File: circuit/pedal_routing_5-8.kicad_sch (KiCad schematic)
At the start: 12 parts, among them U601 CD4051B, U602 CD4051B, U603 CD4051B, U604 CD4051B

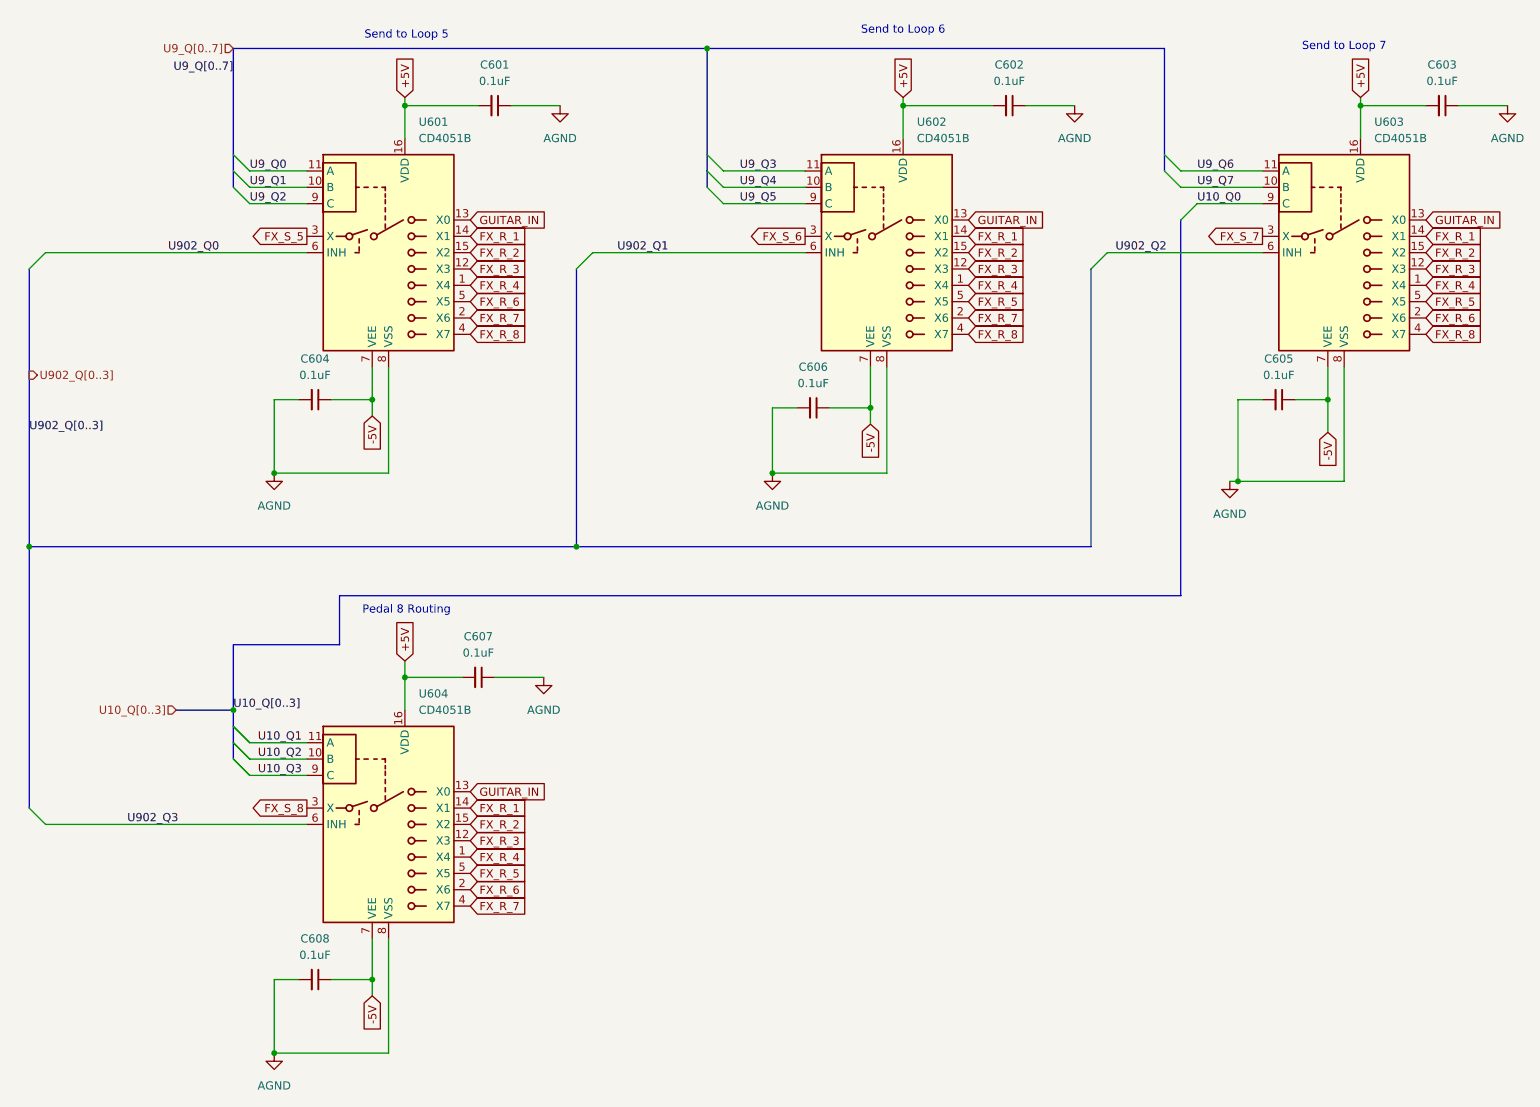
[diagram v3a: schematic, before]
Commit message: Added ferrite beads and tweaked PCB
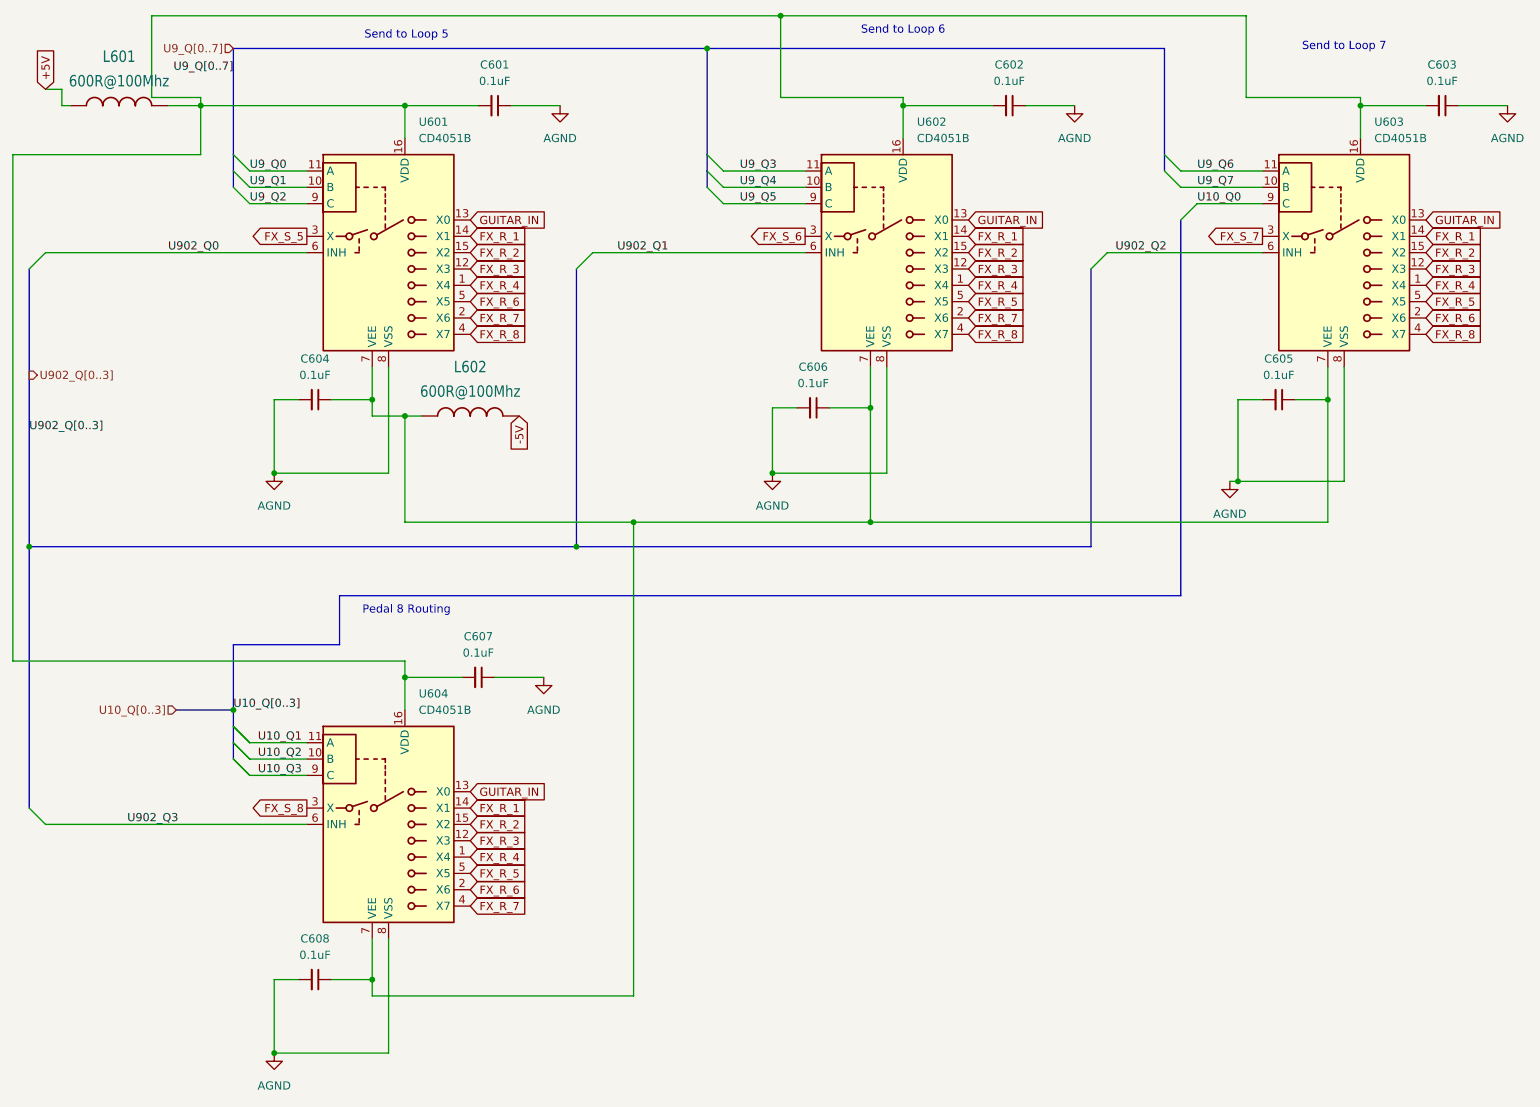
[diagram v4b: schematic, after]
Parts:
- added L601, L602: 600R@100Mhz, WE-UKW:WE-UKW_74275010, symbol WE_UKW:WE-UKW_1SW_74275010
- C601, C602, C603, C604, C605, C606, C607, C608: footprint Capacitor_THT:C_Axial_L3.8mm_D2.6mm_P7.50mm_Horizontal -> Capacitor_THT:C_Disc_D3.0mm_W2.0mm_P2.50mm
- U601, U602, U603, U604: footprint Package_DIP:CERDIP-16_W7.62mm_SideBrazed -> Package_DIP:DIP-16_W7.62mm
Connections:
- net +5V: now also L601.1; no longer C601.2, C602.2, C603.2, C607.2, U601.16 (VDD), U602.16 (VDD), U603.16 (VDD), U604.16 (VDD)
- net -5V: now also L602.2; no longer C604.1, C605.1, C606.1, C608.1, U601.7 (VEE), U602.7 (VEE), U603.7 (VEE), U604.7 (VEE)
- new net: C601.2, C602.2, C603.2, C607.2, L601.2, U601.16 (VDD), U602.16 (VDD), U603.16 (VDD), U604.16 (VDD)
- new net: C604.1, C605.1, C606.1, C608.1, L602.1, U601.7 (VEE), U602.7 (VEE), U603.7 (VEE), U604.7 (VEE)

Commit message: Circuit tweaks and PCB
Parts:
- C601: renamed from C604; footprint Capacitor_THT:C_Disc_D3.0mm_W2.0mm_P2.50mm -> Capacitor_THT:C_Disc_D5.0mm_W2.5mm_P2.50mm
- C602: renamed from C608; footprint Capacitor_THT:C_Disc_D3.0mm_W2.0mm_P2.50mm -> Capacitor_THT:C_Disc_D5.0mm_W2.5mm_P2.50mm
- C603: renamed from C607; footprint Capacitor_THT:C_Disc_D3.0mm_W2.0mm_P2.50mm -> Capacitor_THT:C_Disc_D5.0mm_W2.5mm_P2.50mm
- C604: renamed from C601; footprint Capacitor_THT:C_Disc_D3.0mm_W2.0mm_P2.50mm -> Capacitor_THT:C_Disc_D5.0mm_W2.5mm_P2.50mm
- C605: renamed from C606; footprint Capacitor_THT:C_Disc_D3.0mm_W2.0mm_P2.50mm -> Capacitor_THT:C_Disc_D5.0mm_W2.5mm_P2.50mm
- C606: renamed from C602; footprint Capacitor_THT:C_Disc_D3.0mm_W2.0mm_P2.50mm -> Capacitor_THT:C_Disc_D5.0mm_W2.5mm_P2.50mm
- C607: renamed from C605; footprint Capacitor_THT:C_Disc_D3.0mm_W2.0mm_P2.50mm -> Capacitor_THT:C_Disc_D5.0mm_W2.5mm_P2.50mm
- C608: renamed from C603; footprint Capacitor_THT:C_Disc_D3.0mm_W2.0mm_P2.50mm -> Capacitor_THT:C_Disc_D5.0mm_W2.5mm_P2.50mm
- renumbered U604 to U602, U602 to U603, U603 to U604

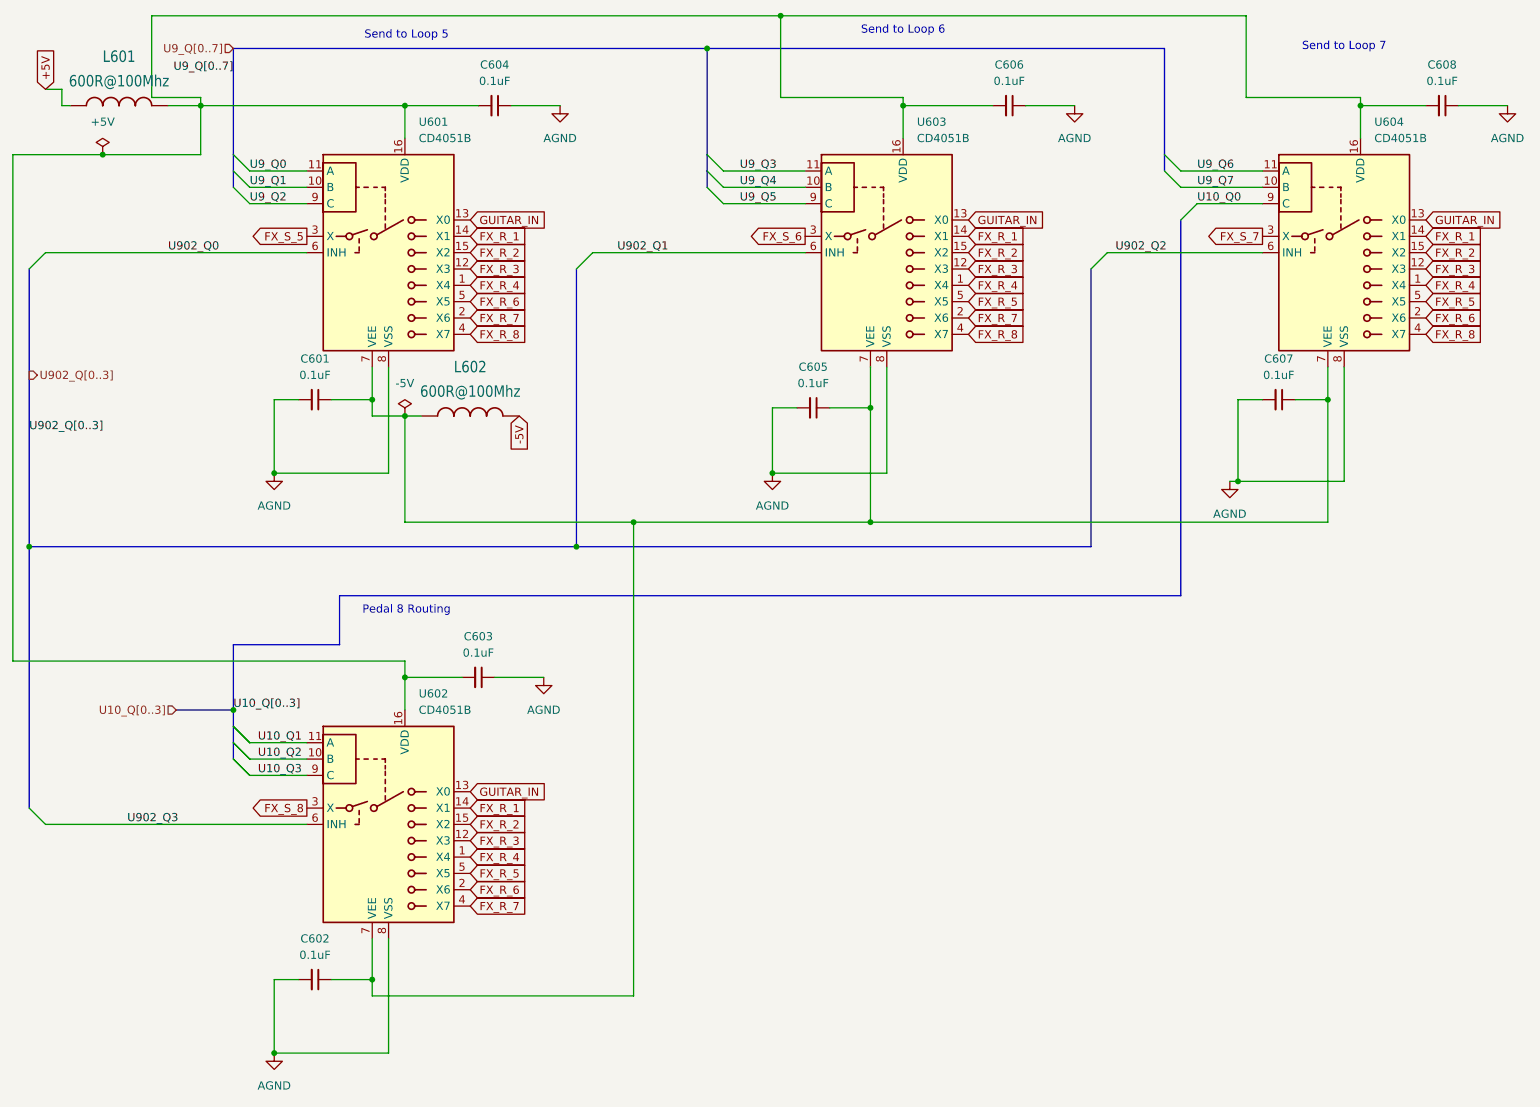
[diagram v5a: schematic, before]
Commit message: Labels for headers on PCB
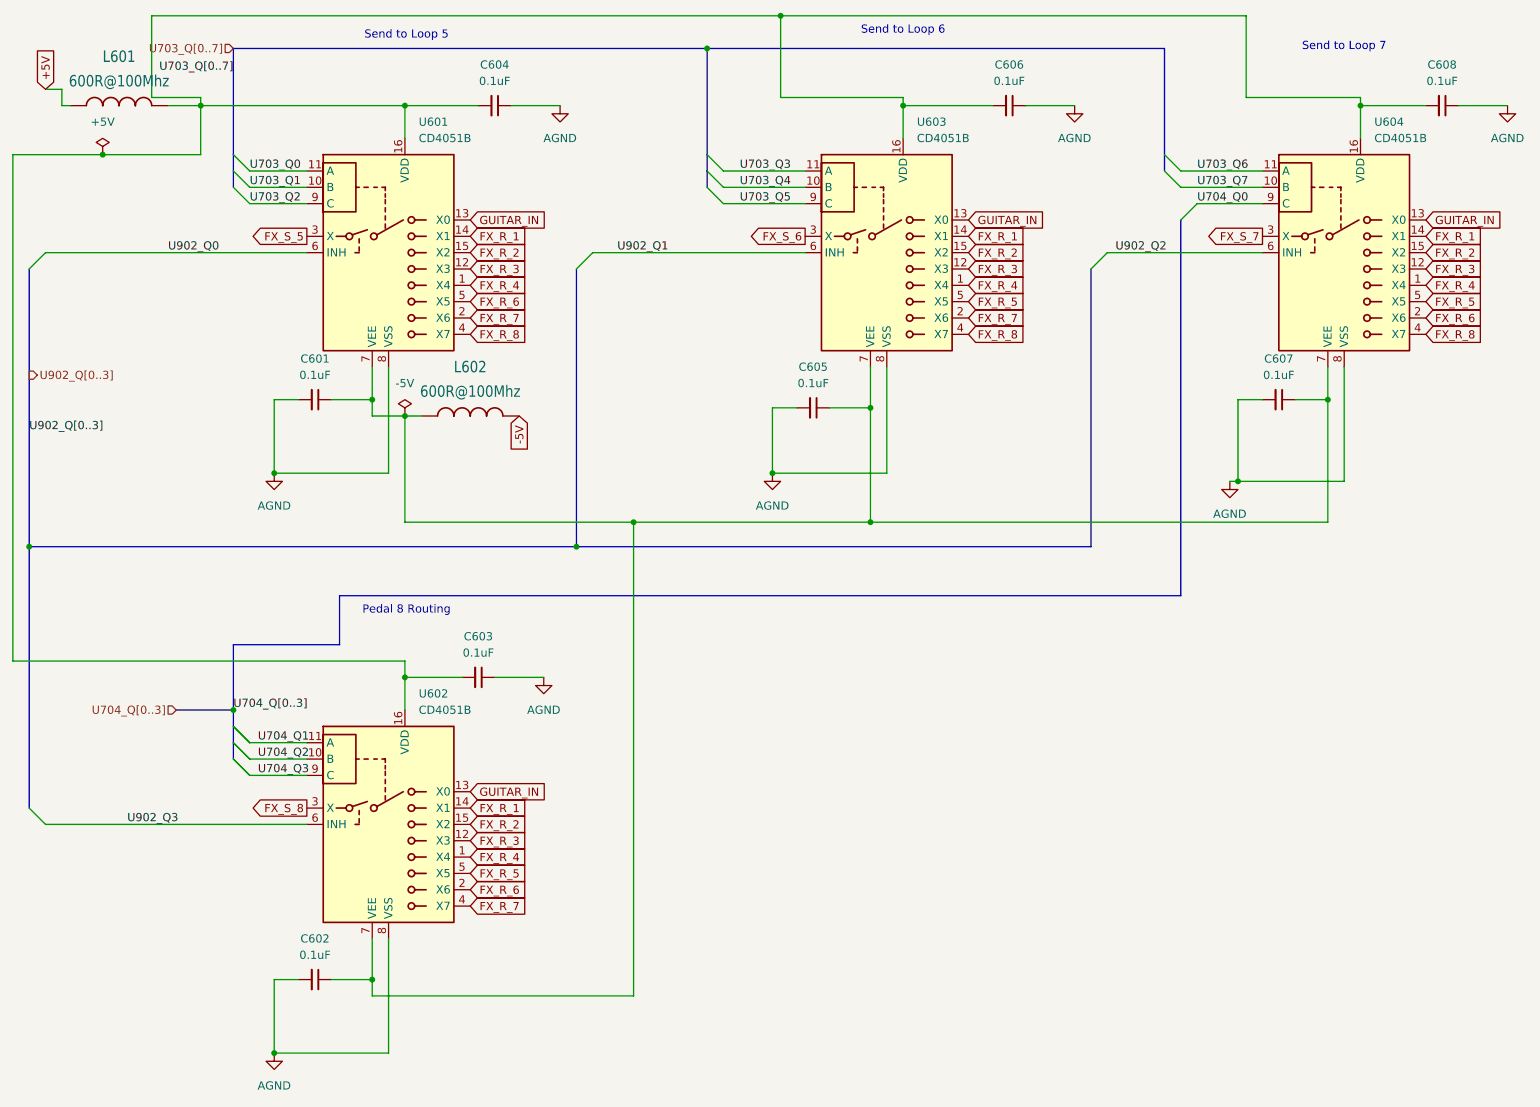
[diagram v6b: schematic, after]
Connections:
- net U10_Q0 renamed U704_Q0
- net U10_Q1 renamed U704_Q1
- net U10_Q2 renamed U704_Q2
- net U10_Q3 renamed U704_Q3
- net U9_Q0 renamed U703_Q0
- net U9_Q1 renamed U703_Q1
- net U9_Q2 renamed U703_Q2
- net U9_Q3 renamed U703_Q3
- net U9_Q4 renamed U703_Q4
- net U9_Q5 renamed U703_Q5
- net U9_Q6 renamed U703_Q6
- net U9_Q7 renamed U703_Q7
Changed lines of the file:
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@@
 		)
 	)
-	(label "U10_Q3"
+	(label "U704_Q3"
 		(at 52.07 132.08 0)
 		(effects
@@
 		)
 	)
-	(label "U9_Q3"
+	(label "U703_Q3"
 		(at 127 38.1 0)
 		(effects
@@
 		)
 	)
-	(label "U9_Q5"
+	(label "U703_Q5"
 		(at 127 43.18 0)
 		(effects
@@
 		)
 	)
-	(label "U10_Q[0..3]"
+	(label "U704_Q[0..3]"
 		(at 48.26 121.92 0)
 		(effects
@@
 		)
 	)
-	(label "U9_Q7"
+	(label "U703_Q7"
 		(at 198.12 40.64 0)
 		(effects
@@
 		)
 	)
-	(label "U9_Q[0..7]"
+	(label "U703_Q[0..7]"
 		(at 48.26 22.86 180)
 		(effects
@@
 		)
 	)
-	(label "U9_Q4"
+	(label "U703_Q4"
 		(at 127 40.64 0)
 		(effects
@@
 		)
 	)
-	(label "U10_Q0"
+	(label "U704_Q0"
 		(at 198.12 43.18 0)
 		(effects
@@
 		)
 	)
-	(label "U9_Q6"
+	(label "U703_Q6"
 		(at 198.12 38.1 0)
 		(effects
@@
 		)
 	)
-	(label "U9_Q1"
+	(label "U703_Q1"
 		(at 50.8 40.64 0)
 		(effects
@@
 		)
 	)
-	(label "U10_Q1"
+	(label "U704_Q1"
 		(at 52.07 127 0)
 		(effects
@@
 		)
 	)
-	(label "U9_Q0"
+	(label "U703_Q0"
 		(at 50.8 38.1 0)
 		(effects
@@
 		)
 	)
-	(label "U10_Q2"
+	(label "U704_Q2"
 		(at 52.07 129.54 0)
 		(effects
@@
 		)
 	)
-	(label "U9_Q2"
+	(label "U703_Q2"
 		(at 50.8 43.18 0)
 		(effects
@@
 		)
 	)
-	(hierarchical_label "U10_Q[0..3]"
+	(hierarchical_label "U704_Q[0..3]"
 		(shape input)
 		(at 39.37 121.92 180)
@@
 		)
 	)
-	(hierarchical_label "U9_Q[0..7]"
+	(hierarchical_label "U703_Q[0..7]"
 		(shape input)
 		(at 48.26 19.05 180)
